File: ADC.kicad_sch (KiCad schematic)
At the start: 1 part, among them IC1 ADS1256IDBRG4

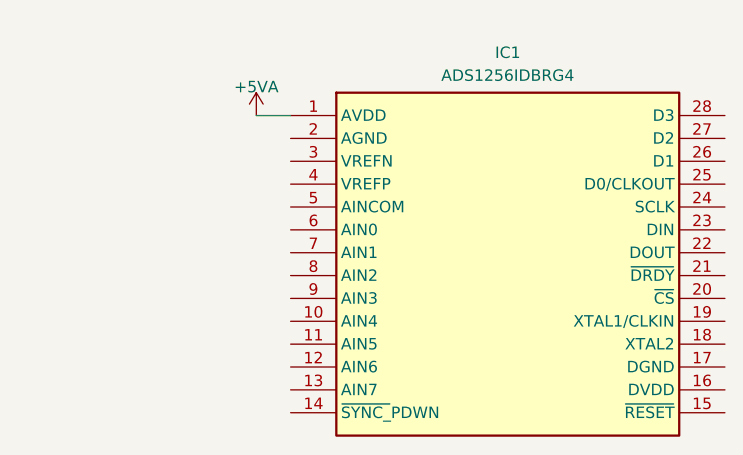
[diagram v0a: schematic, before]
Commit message: switch to external ADC, switch to amp superseal 1.0 for connector, need to check CANFD pins disagreement with datasheet
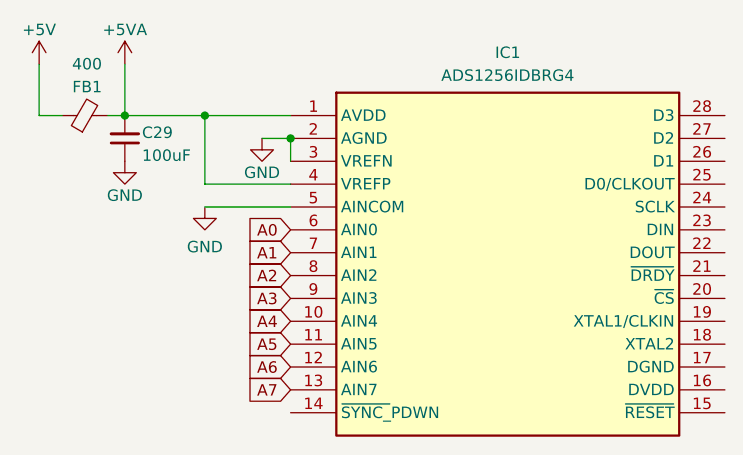
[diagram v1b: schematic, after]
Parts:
- added C29: 100uF, Capacitor_SMD:C_0805_2012Metric, symbol Device:C_Small
- added FB1: 400, Resistor_SMD:R_0603_1608Metric, symbol Device:FerriteBead_Small
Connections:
- net +5VA: now also IC1.4 (VREFP), C29.2, FB1.2
- net A4: now reaches IC1.10 (AIN4)
- net A5: now reaches IC1.11 (AIN5)
- net A6: now reaches IC1.12 (AIN6)
- net A7: now reaches IC1.13 (AIN7)
- net GND: now reaches IC1.2 (AGND)
- net GND: now also IC1.3 (VREFN), IC1.5 (AINCOM), C29.1
- net A0: now reaches IC1.6 (AIN0)
- net A1: now reaches IC1.7 (AIN1)
- net A2: now reaches IC1.8 (AIN2)
- net A3: now reaches IC1.9 (AIN3)
- new net +5V: FB1.1
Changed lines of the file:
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@@
 (kicad_sch (version 20230121) (generator eeschema)
   (paper "A4")
-  (wire (pts (xy 112.395 75.565) (xy 116.205 75.565))
-    (stroke (width 0) (type default))
-  )
-  (symbol (lib_id "power:+5VA") (at 112.395 75.565 0) (unit 1)
-    (in_bom yes) (on_board yes) (dnp no) (fields_autoplaced)
-    (property "Reference" "#PWR021" (at 112.395 79.375 0)
-      (effects (font (size 1.27 1.27)) hide)
-    )
-    (property "Value" "+5VA" (at 112.395 72.39 0)
-      (effects (font (size 1.27 1.27)))
-    )
-    (property "Footprint" "" (at 112.395 75.565 0)
-      (effects (font (size 1.27 1.27)) hide)
-    )
-    (property "Datasheet" "" (at 112.395 75.565 0)
+  (junction (at 116.205 78.105) (diameter 0) (color 0 0 0 0)
+  )
+  (junction (at 97.79 75.565) (diameter 0) (color 0 0 0 0)
+  )
+  (junction (at 106.68 75.565) (diameter 0) (color 0 0 0 0)
+  )
+  (wire (pts (xy 106.68 75.565) (xy 106.68 83.185))
+    (stroke (width 0) (type default))
+  )
+  (wire (pts (xy 88.265 75.565) (xy 90.805 75.565))
+    (stroke (width 0) (type default))
+  )
+  (wire (pts (xy 106.68 85.725) (xy 116.205 85.725))
+    (stroke (width 0) (type default))
+  )
+  (wire (pts (xy 116.205 83.185) (xy 106.68 83.185))
+    (stroke (width 0) (type default))
+  )
+  (wire (pts (xy 116.205 78.105) (xy 116.205 80.645))
+    (stroke (width 0) (type default))
+  )
+  (wire (pts (xy 106.68 75.565) (xy 116.205 75.565))
+    (stroke (width 0) (type default))
+  )
+  (wire (pts (xy 95.885 75.565) (xy 97.79 75.565))
+    (stroke (width 0) (type default))
+  )
+  (wire (pts (xy 113.03 78.105) (xy 116.205 78.105))
+    (stroke (width 0) (type default))
+  )
+  (wire (pts (xy 97.79 69.85) (xy 97.79 75.565))
+    (stroke (width 0) (type default))
+  )
+  (wire (pts (xy 97.79 75.565) (xy 106.68 75.565))
+    (stroke (width 0) (type default))
+  )
+  (wire (pts (xy 88.265 69.85) (xy 88.265 75.565))
+    (stroke (width 0) (type default))
+  )
+  (global_label "A6" (shape input) (at 116.205 103.505 180) (fields_autoplaced)
+    (effects (font (size 1.27 1.27)) (justify right))
+    (property "Intersheetrefs" "${INTERSHEET_REFS}" (at 111.0011 103.505 0)
+      (effects (font (size 1.27 1.27)) (justify right) hide)
+    )
+  )
+  (global_label "A5" (shape input) (at 116.205 100.965 180) (fields_autoplaced)
+    (effects (font (size 1.27 1.27)) (justify right))
+    (property "Intersheetrefs" "${INTERSHEET_REFS}" (at 111.0011 100.965 0)
+      (effects (font (size 1.27 1.27)) (justify right) hide)
+    )
+  )
+  (global_label "A3" (shape input) (at 116.205 95.885 180) (fields_autoplaced)
+    (effects (font (size 1.27 1.27)) (justify right))
+    (property "Intersheetrefs" "${INTERSHEET_REFS}" (at 111.0011 95.885 0)
+      (effects (font (size 1.27 1.27)) (justify right) hide)
+    )
+  )
+  (global_label "A0" (shape input) (at 116.205 88.265 180) (fields_autoplaced)
+    (effects (font (size 1.27 1.27)) (justify right))
+    (property "Intersheetrefs" "${INTERSHEET_REFS}" (at 111.0011 88.265 0)
+      (effects (font (size 1.27 1.27)) (justify right) hide)
+    )
+  )
+  (global_label "A4" (shape input) (at 116.205 98.425 180) (fields_autoplaced)
+    (effects (font (size 1.27 1.27)) (justify right))
+    (property "Intersheetrefs" "${INTERSHEET_REFS}" (at 111.0011 98.425 0)
+      (effects (font (size 1.27 1.27)) (justify right) hide)
+    )
+  )
+  (global_label "A7" (shape input) (at 116.205 106.045 180) (fields_autoplaced)
+    (effects (font (size 1.27 1.27)) (justify right))
+    (property "Intersheetrefs" "${INTERSHEET_REFS}" (at 111.0011 106.045 0)
+      (effects (font (size 1.27 1.27)) (justify right) hide)
+    )
+  )
+  (global_label "A1" (shape input) (at 116.205 90.805 180) (fields_autoplaced)
+    (effects (font (size 1.27 1.27)) (justify right))
+    (property "Intersheetrefs" "${INTERSHEET_REFS}" (at 111.0011 90.805 0)
+      (effects (font (size 1.27 1.27)) (justify right) hide)
+    )
+  )
+  (global_label "A2" (shape input) (at 116.205 93.345 180) (fields_autoplaced)
+    (effects (font (size 1.27 1.27)) (justify right))
+    (property "Intersheetrefs" "${INTERSHEET_REFS}" (at 111.0011 93.345 0)
+      (effects (font (size 1.27 1.27)) (justify right) hide)
+    )
+  )
+  (symbol (lib_id "Device:FerriteBead_Small") (at 93.345 75.565 90) (unit 1)
+    (in_bom yes) (on_board yes) (dnp no)
+    (property "Reference" "FB1" (at 95.25 72.39 90)
+      (effects (font (size 1.27 1.27)) (justify left))
+    )
+    (property "Value" "400" (at 95.25 69.85 90)
+      (effects (font (size 1.27 1.27)) (justify left))
+    )
+    (property "Footprint" "Resistor_SMD:R_0603_1608Metric" (at 93.345 77.343 90)
+      (effects (font (size 1.27 1.27)) hide)
+    )
+    (property "Datasheet" "https://www.mouser.com/datasheet/2/418/8/ENG_DS_1773178_1_B-2940935.pdf" (at 93.345 75.565 0)
+      (effects (font (size 1.27 1.27)) hide)
+    )
+    (pin "1")
+    (pin "2")
+    (instances
+      (project "scr23-sens-to-can"
+        (path "/9d4a62b8-9a16-4c8d-8b16-7072bfb3ee3d"
+          (reference "FB1") (unit 1)
+        )
+        (path "/9d4a62b8-9a16-4c8d-8b16-7072bfb3ee3d/a8dca7ff-e971-4605-965d-4f74c3dd69be"
+          (reference "FB2") (unit 1)
+        )
+      )
+    )
+  )
+  (symbol (lib_id "power:+5VA") (at 97.79 69.85 0) (unit 1)
+    (in_bom yes) (on_board yes) (dnp no)
+    (property "Reference" "#PWR021" (at 97.79 73.66 0)
+      (effects (font (size 1.27 1.27)) hide)
+    )
+    (property "Value" "+5VA" (at 97.79 66.04 0)
+      (effects (font (size 1.27 1.27)))
+    )
+    (property "Footprint" "" (at 97.79 69.85 0)
+      (effects (font (size 1.27 1.27)) hide)
+    )
+    (property "Datasheet" "" (at 97.79 69.85 0)
       (effects (font (size 1.27 1.27)) hide)
     )
@@
         (path "/9d4a62b8-9a16-4c8d-8b16-7072bfb3ee3d/a8dca7ff-e971-4605-965d-4f74c3dd69be"
           (reference "#PWR021") (unit 1)
+        )
+      )
+    )
+  )
+  (symbol (lib_id "Device:C_Small") (at 97.79 78.105 180) (unit 1)
+    (in_bom yes) (on_board yes) (dnp no)
+    (property "Reference" "C29" (at 99.695 77.47 0)
+      (effects (font (size 1.27 1.27)) (justify right))
+    )
+    (property "Value" "100uF" (at 99.695 80.01 0)
+      (effects (font (size 1.27 1.27)) (justify right))
+    )
+    (property "Footprint" "Capacitor_SMD:C_0805_2012Metric" (at 97.79 78.105 0)
+      (effects (font (size 1.27 1.27)) hide)
+    )
+    (property "Datasheet" "~" (at 97.79 78.105 0)
+      (effects (font (size 1.27 1.27)) hide)
+    )
+    (pin "1")
+    (pin "2")
+    (instances
+      (project "scr23-sens-to-can"
+        (path "/9d4a62b8-9a16-4c8d-8b16-7072bfb3ee3d/a8dca7ff-e971-4605-965d-4f74c3dd69be"
+          (reference "C29") (unit 1)
         )
       )
@@
         )
       )
+    )
+  )
+  (symbol (lib_id "power:GND") (at 97.79 80.645 0) (unit 1)
+    (in_bom yes) (on_board yes) (dnp no)
+    (property "Reference" "#PWR030" (at 97.79 86.995 0)
+      (effects (font (size 1.27 1.27)) hide)
+    )
+    (property "Value" "GND" (at 97.79 84.455 0)
+      (effects (font (size 1.27 1.27)))
+    )
+    (property "Footprint" "" (at 97.79 80.645 0)
+      (effects (font (size 1.27 1.27)) hide)
+    )
+    (property "Datasheet" "" (at 97.79 80.645 0)
+      (effects (font (size 1.27 1.27)) hide)
+    )
+    (pin "1")
+    (instances
+      (project "scr23-sens-to-can"
+        (path "/9d4a62b8-9a16-4c8d-8b16-7072bfb3ee3d/a8dca7ff-e971-4605-965d-4f74c3dd69be"
+          (reference "#PWR030") (unit 1)
+        )
+      )
+    )
+  )
+  (symbol (lib_id "power:+5V") (at 88.265 69.85 0) (unit 1)
+    (in_bom yes) (on_board yes) (dnp no)
+    (property "Reference" "#PWR029" (at 88.265 73.66 0)
+      (effects (font (size 1.27 1.27)) hide)
+    )
+    (property "Value" "+5V" (at 88.265 66.04 0)
+      (effects (font (size 1.27 1.27)))
+    )
+    (property "Footprint" "" (at 88.265 69.85 0)
+      (effects (font (size 1.27 1.27)) hide)
+    )
+    (property "Datasheet" "" (at 88.265 69.85 0)
+      (effects (font (size 1.27 1.27)) hide)
+    )
+    (pin "1")
+    (instances
+      (project "scr23-sens-to-can"
+        (path "/9d4a62b8-9a16-4c8d-8b16-7072bfb3ee3d/a8dca7ff-e971-4605-965d-4f74c3dd69be"
+          (reference "#PWR029") (unit 1)
+        )
+      )
+    )
+  )
+  (symbol (lib_id "power:GND") (at 113.03 78.105 0) (unit 1)
+    (in_bom yes) (on_board yes) (dnp no)
+    (property "Reference" "#PWR034" (at 113.03 84.455 0)
+      (effects (font (size 1.27 1.27)) hide)
+    )
+    (property "Value" "GND" (at 113.03 81.915 0)
+      (effects (font (size 1.27 1.27)))
+    )
+    (property "Footprint" "" (at 113.03 78.105 0)
+      (effects (font (size 1.27 1.27)) hide)
+    )
+    (property "Datasheet" "" (at 113.03 78.105 0)
+      (effects (font (size 1.27 1.27)) hide)
+    )
+    (pin "1")
+    (instances
+      (project "scr23-sens-to-can"
+        (path "/9d4a62b8-9a16-4c8d-8b16-7072bfb3ee3d/a8dca7ff-e971-4605-965d-4f74c3dd69be"
+          (reference "#PWR034") (unit 1)
+        )
+      )
+    )
+  )
+  (symbol (lib_id "power:GND") (at 106.68 85.725 0) (unit 1)
+    (in_bom yes) (on_board yes) (dnp no) (fields_autoplaced)
+    (property "Reference" "#PWR035" (at 106.68 92.075 0)
+      (effects (font (size 1.27 1.27)) hide)
+    )
+    (property "Value" "GND" (at 106.68 90.17 0)
+      (effects (font (size 1.27 1.27)))
+    )
+    (property "Footprint" "" (at 106.68 85.725 0)
+      (effects (font (size 1.27 1.27)) hide)
+    )
+    (property "Datasheet" "" (at 106.68 85.725 0)
+      (effects (font (size 1.27 1.27)) hide)
+    )
+    (pin "1")
+    (instances
+      (project "scr23-sens-to-can"
+        (path "/9d4a62b8-9a16-4c8d-8b16-7072bfb3ee3d/a8dca7ff-e971-4605-965d-4f74c3dd69be"
+          (reference "#PWR035") (unit 1)
+        )
+      )
